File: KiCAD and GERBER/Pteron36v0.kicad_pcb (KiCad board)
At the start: 2 copper layers, 140.1 x 108.1 mm, 62 parts, among them J1 AudioJack4, J2 AudioJack4, J3 Conn_01x04, SW10 SW_PUSH, SW12 SW_PUSH, SW13 SW_PUSH, SW14 SW_PUSH, SW15 SW_PUSH, SW17 SW_PUSH, SW18 SW_PUSH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

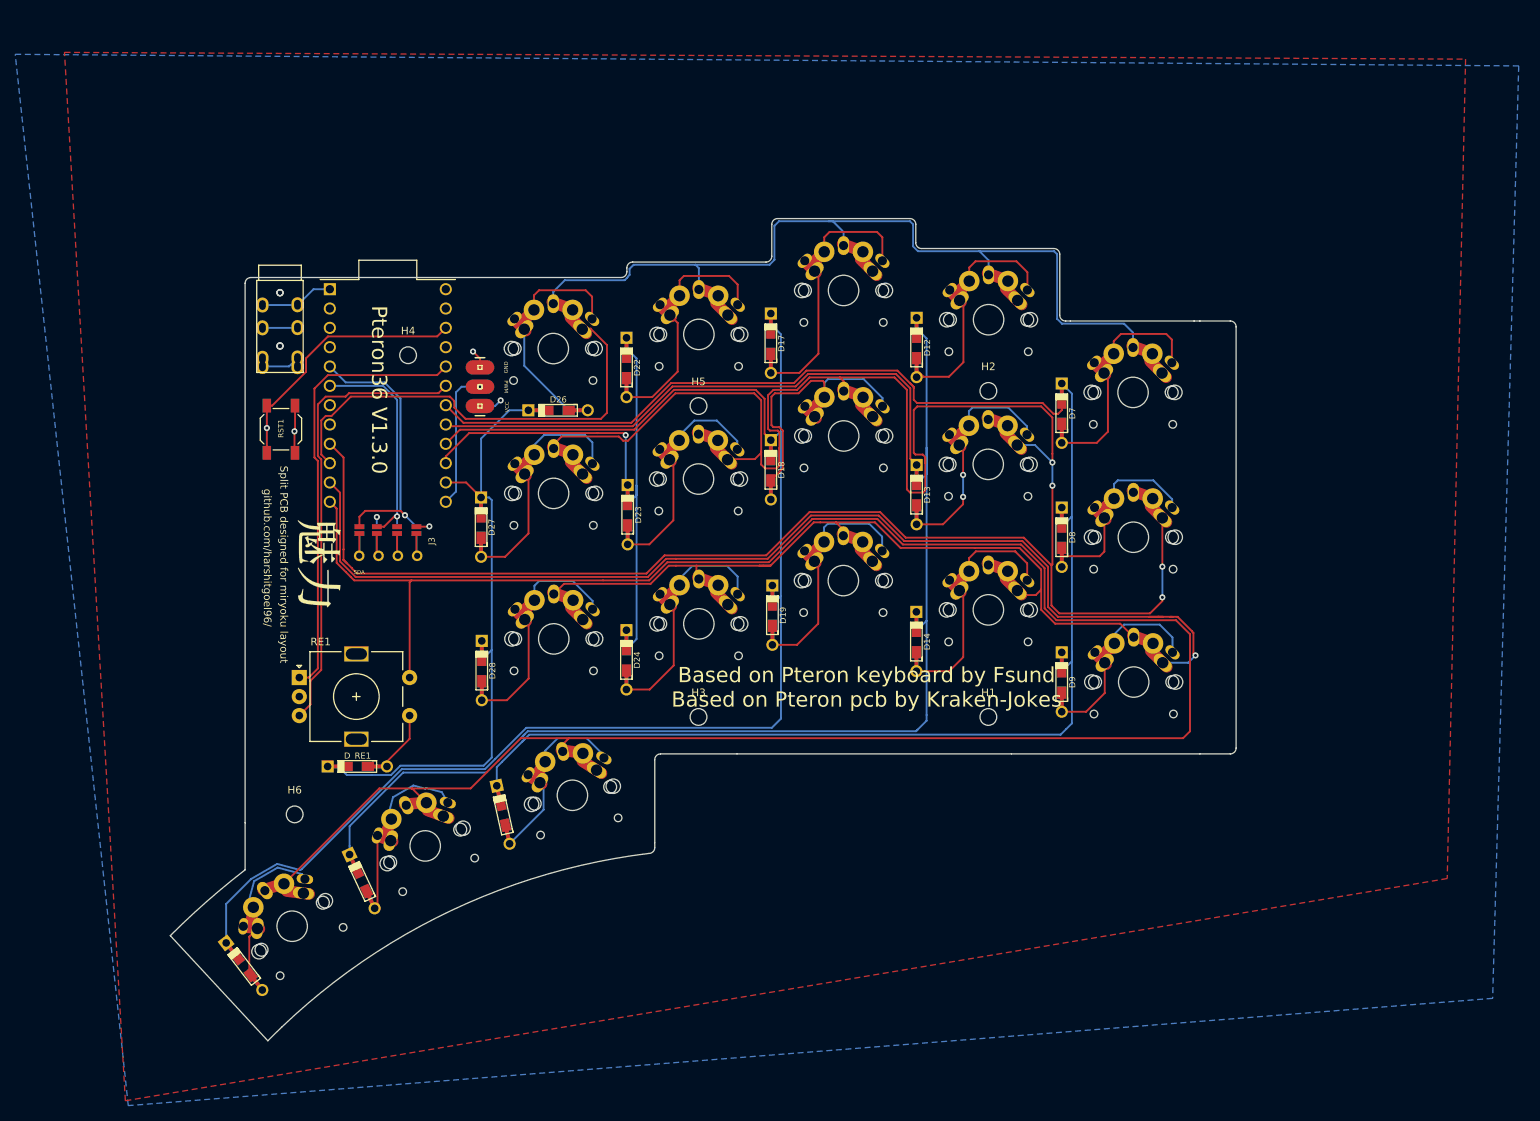
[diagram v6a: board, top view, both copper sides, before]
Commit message: clean up pads
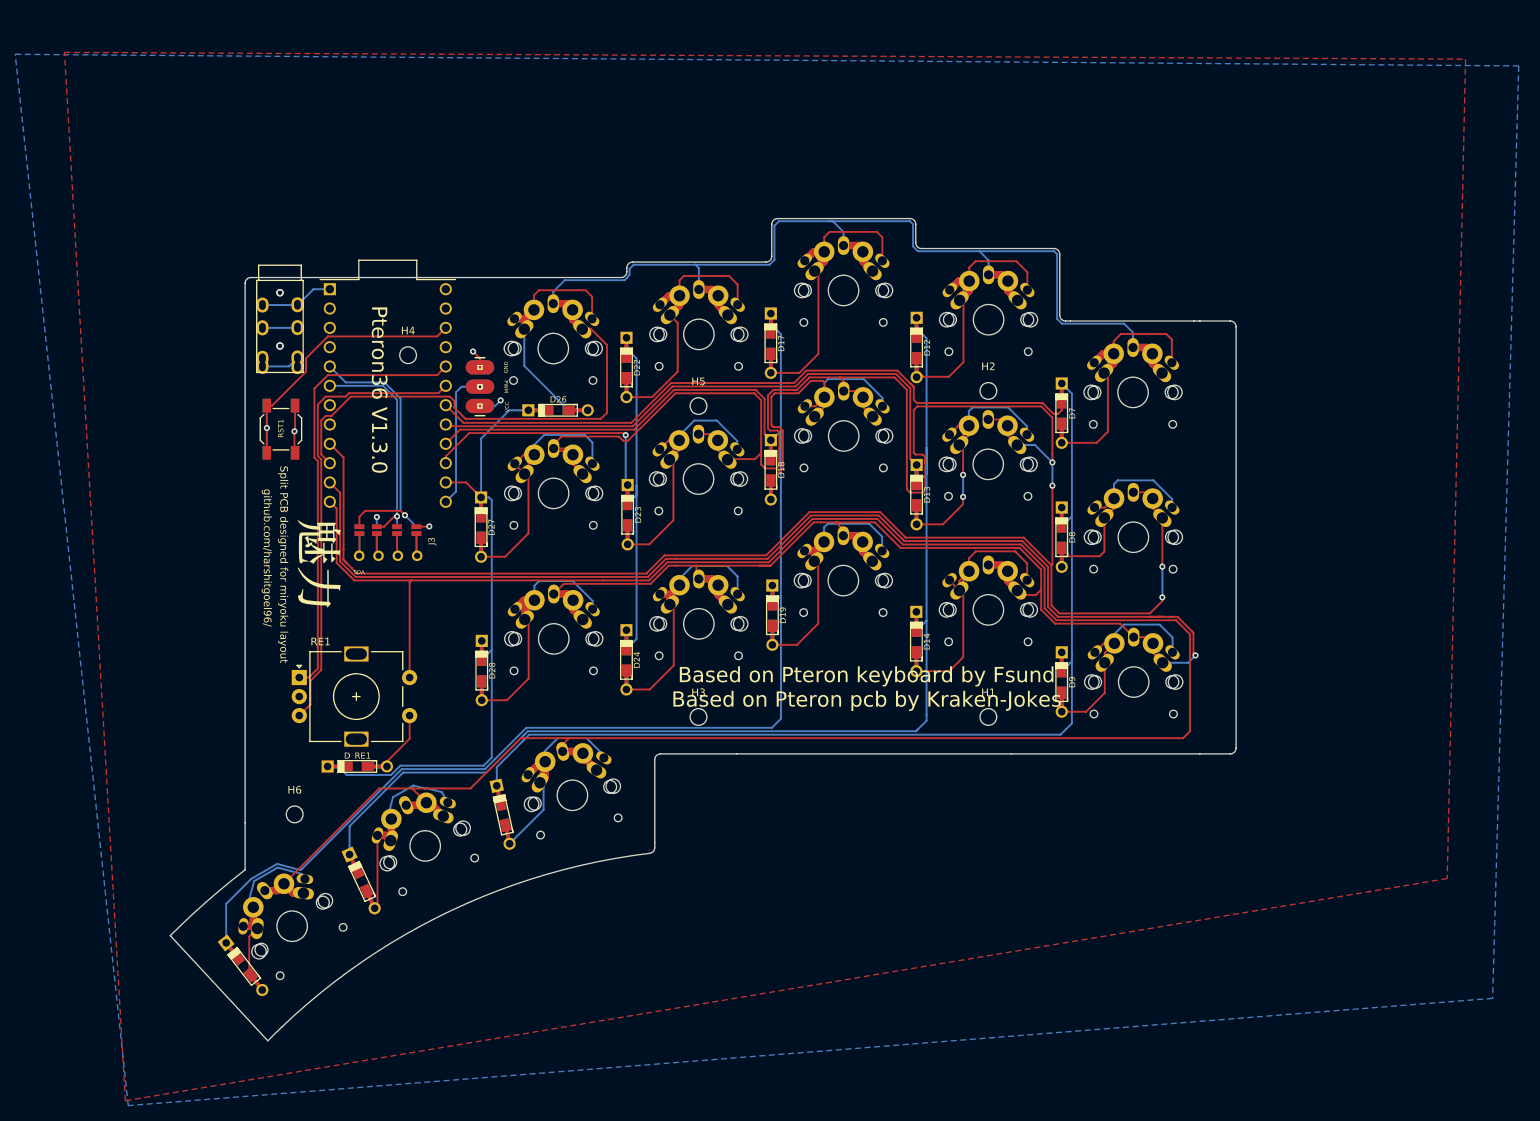
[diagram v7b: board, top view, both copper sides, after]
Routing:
- net /Row2: track 302.5 -> 332.3 mm
- net /Row1: track 171.5 -> 201.2 mm
- net /Row3: track 248.0 -> 277.8 mm
- net /Row4: track 292.0 -> 309.4 mm
- net Net-(D23-Pad2): track 28.4 -> 34.5 mm
- net Net-(D8-Pad2): track 22.2 -> 28.3 mm
- net Net-(D12-Pad2): track 30.4 -> 36.5 mm
- net Net-(D22-Pad2): track 29.0 -> 35.1 mm
- net Net-(D17-Pad2): track 33.2 -> 39.3 mm
- net Net-(D13-Pad2): track 29.7 -> 35.8 mm
- net Net-(D28-Pad2): track 28.9 -> 35.0 mm
- net Net-(D18-Pad2): track 35.5 -> 41.7 mm
- net Net-(D7-Pad2): track 29.9 -> 36.0 mm
- net Net-(D9-Pad2): track 22.7 -> 28.8 mm
- net Net-(D10-Pad2): track 23.4 -> 29.4 mm
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
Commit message: keebio footprint
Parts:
- SW10, SW12, SW13, SW14, SW15, SW17, SW18, SW19, SW20, SW22, SW23, SW24, SW26, SW27, SW28, SW7, SW8, SW9: footprint User-Submitted:uni-new -> Keebio-Parts:Triple-Dual-1u-LED
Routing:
- net /Row2: track 332.3 -> 333.9 mm
- net /Row1: track 201.2 -> 202.0 mm
